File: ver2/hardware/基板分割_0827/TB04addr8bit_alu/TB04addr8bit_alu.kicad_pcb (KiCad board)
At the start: 2 copper layers, 125 x 135 mm, 102 parts, among them IC201 74HC161N, IC202 74HC161N, IC203 74HC161N, IC204 74HC161N, IC301 74HC161N, IC302 74HC161N, IC303 74HC161N, IC304 74HC161N, J1602 Screw_Terminal_01x02, J2 Conn_02x20_Odd_Even, J3 Conn_02x10_Odd_Even, J601 Conn_02x05_Odd_Even, U102 74HC138, U201 74HC253, U202 74HC253, U203 74HC253, U204 74HC253, U301 74HC253, U302 74HC253, U303 74HC253, U304 74HC253, U402 74HC253, U403 74HC253, U405 74HC253, U406 74HC253, U603 28C256, U605 74HC74, U702 74HC273, U704 28C256

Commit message: ver2: 3枚の外形を高さ150mmに統一／制御板のプルダウンをSIP集約・取付穴2個追加(配置は途中)
- 外形: 演算130x150・制御200x150・IF135x150
- 制御板: R603-R606(10K x4)をRN602(R_Array_SIP5)へ集約／取付穴H105・H106を追加／U1101のフットプリントをDIP-24_W15.24mm_Socketへ
- 検証: 署名変化は制御8ピン(ネット名のみ・構成員同一)と演算32ピン(同値素子の割り当て替え)だけ／未接続入力0・単一構成員ネット0・回路図とPCBの参照番号差分0
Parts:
- moved C703 275.1 mm to (108.0, 184.0), turned to 90 degrees
- moved C704 266.4 mm to (123.4, 170.4), turned to 90 degrees
- moved U704 265.8 mm to (112.6, 192.6), turned to 90 degrees
- moved U702 259.2 mm to (128.0, 172.6), turned to 90 degrees
- moved J3 249.5 mm to (104.0, 157.8), turned to 180 degrees
- moved J2 236.1 mm to (106.4, 70.0)
- moved J601 204.8 mm to (108.0, 168.4), turned to 90 degrees
- moved D601 171.7 mm to (154.0, 193.4), turned to 90 degrees
- moved D602 164.7 mm to (160.0, 193.4), turned to 90 degrees
- moved R601 162.7 mm to (154.0, 180.8), turned to -90 degrees
- moved C608 161.6 mm to (155.6, 170.5), turned to 90 degrees
- moved U102 159.4 mm to (202.0, 157.0), turned to 90 degrees
- moved R602 156.6 mm to (160.0, 180.8), turned to -90 degrees
- moved U605 152.7 mm to (158.4, 172.6), turned to 90 degrees
- moved C601 149.9 mm to (166.8, 185.3), turned to 90 degrees
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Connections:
- RN201 pad 2: Net-(D201-K) -> Net-(D209-K)
- RN201 pad 3: Net-(D203-K) -> Net-(D211-K)
- RN201 pad 4: Net-(D205-K) -> Net-(D213-K)
- RN201 pad 5: Net-(D207-K) -> Net-(D215-K)
- RN201 pad 6: Net-(D209-K) -> Net-(D201-K)
- RN201 pad 7: Net-(D211-K) -> Net-(D203-K)
- RN201 pad 8: Net-(D213-K) -> Net-(D205-K)
- RN201 pad 9: Net-(D215-K) -> Net-(D207-K)
- RN202 pad 2: Net-(D202-K) -> Net-(D210-K)
- RN202 pad 3: Net-(D204-K) -> Net-(D212-K)
- RN202 pad 4: Net-(D206-K) -> Net-(D214-K)
- RN202 pad 5: Net-(D208-K) -> Net-(D216-K)
- RN202 pad 6: Net-(D210-K) -> Net-(D202-K)
- RN202 pad 7: Net-(D212-K) -> Net-(D204-K)
- RN202 pad 8: Net-(D214-K) -> Net-(D206-K)
- RN202 pad 9: Net-(D216-K) -> Net-(D208-K)
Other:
- board size 125 x 135 mm -> 130 x 150 mm

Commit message: ver2: 制御板の配置をユーザーが調整／演算板のD209を移動(配線前)
- 制御板: 66部品を移動(09-01の再配置に対する手直し)。回転の変更なし
- 演算板: D209のみ移動
- 検査: 2枚ともパッドの外形外0・パッド→ネットの変化0・配線0
  制御板 courtyard重なり0 / 演算板は既知のC608-U605(0.06x7.19mm)のみ
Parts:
- moved D209 3.16 mm to (175.6, 143.0)
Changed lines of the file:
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@@
 	(footprint "LED_THT:LED_D3.0mm_Clear"
 		(layer "F.Cu")
-		(at 172.62 144 90)
+		(at 175.62 143 90)
 		(descr "LED, diameter 3.0mm, 2 pins, clear, generated by kicad-footprint-generator")
 		(tags "LED")
@@
 		)
 		(point
-			(at 172.62 142.73)
+			(at 175.62 141.73)
 			(size 2)
 			(layer "F.Fab")

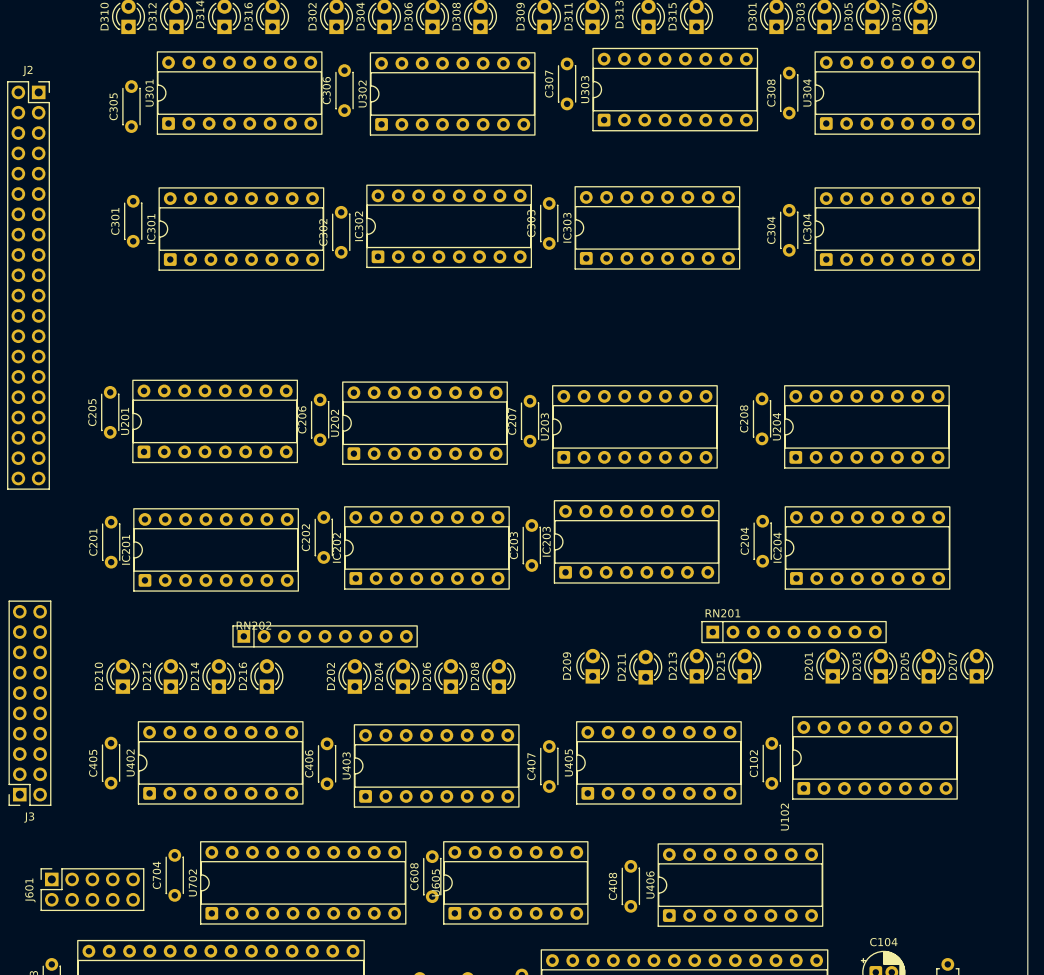
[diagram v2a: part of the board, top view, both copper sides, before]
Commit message: ver2: 演算板の配置を組み直し(配線長-6.7%%・交差-18.4%%・反転2個)
MUXの対(U201-U203/U202-U204)を隣接させ、DOa/DObが縦に降りる並びに変更。
全23ICのピン1を2.54mmグリッドに整合。固定部品(コネクタ・LED・28C256)は不動。
検証: パッド外形外0/courtyard重なり0/固定部品移動0/パッド-ネット変化0/DRCはシルク6件のみ。
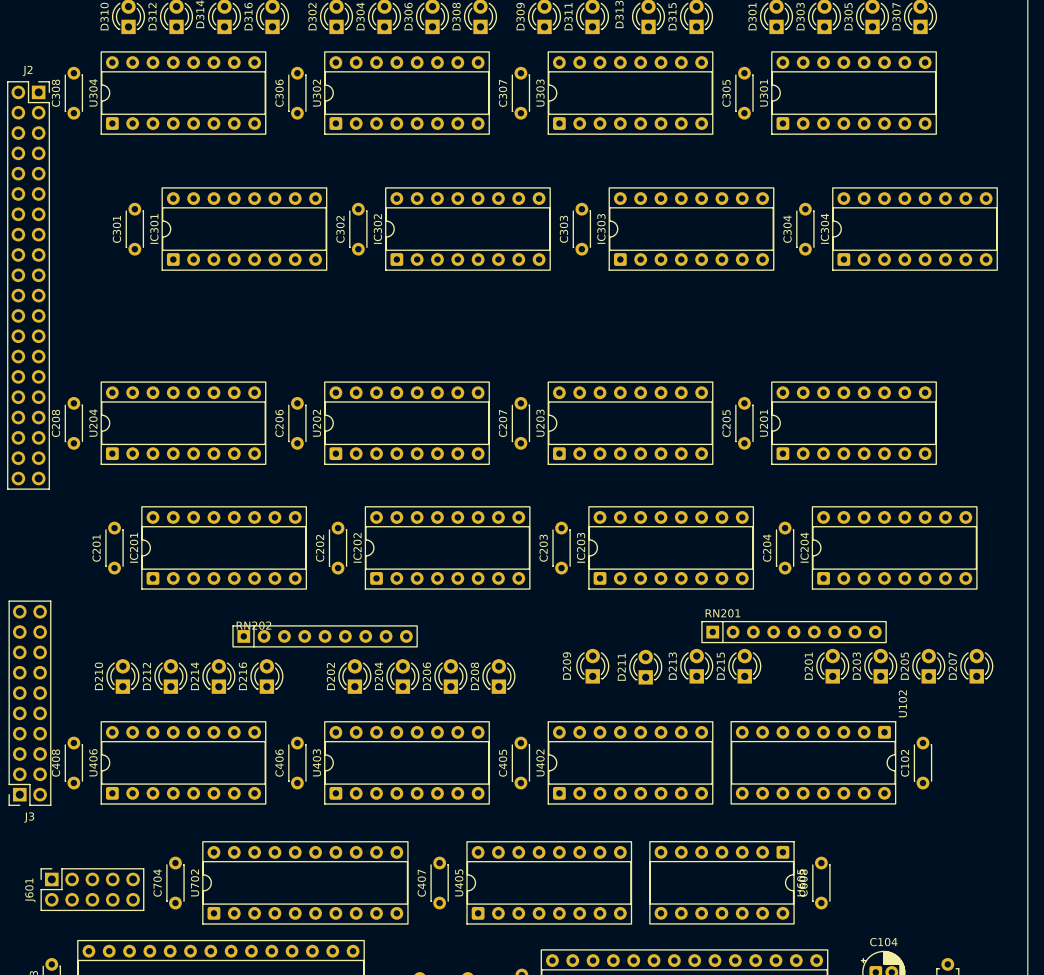
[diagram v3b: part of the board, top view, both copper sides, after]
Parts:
- moved C308 89.4 mm to (110.8, 72.6)
- moved U304 89.2 mm to (115.6, 73.9)
- moved C208 86.0 mm to (110.8, 113.9)
- moved U204 85.4 mm to (115.6, 115.2)
- moved U201 79.9 mm to (199.4, 115.2)
- moved C205 79.3 mm to (194.6, 113.9)
- moved U301 76.8 mm to (199.4, 73.9)
- moved C305 76.6 mm to (194.6, 72.6)
- moved C408 71.3 mm to (110.8, 156.3)
- moved U406 71.3 mm to (115.6, 157.6)
- moved C405 51.2 mm to (166.6, 156.3)
- moved U402 51.2 mm to (171.4, 157.6)
- moved C608 48.6 mm to (204.2, 171.3)
- moved U605 41.7 mm to (199.4, 165.0), turned to -90 degrees
- moved U405 20.3 mm to (161.3, 172.6)
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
